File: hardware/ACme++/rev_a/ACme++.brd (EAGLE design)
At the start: 72.6 x 47.1 mm, 52 parts, among them J1 AC-PLUG, J2 WIRE_HOLE-14AWG, J4 WIRE_HOLE-14AWG, J5 WIRE_HOLE-14AWG, K1 S216S01F, Q1 STGD5NB120SZT4, Q2 FDV301N, U1 ADE7753, U2 SR086SG-G, U3 TDA3664AT, X1 ECS-35-17-5PX-TR

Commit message: working on routing
power supply laid out

working on ace

lots of room...put cc2538 on this board? hard to argue not to...
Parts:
- moved X1 29.0 mm to (15.2, 17.8)
- moved L3 25.2 mm to (34.8, 45.6), turned to 180 degrees
- moved R15 23.4 mm to (46.1, 37.7), turned to 180 degrees
- moved L4 22.7 mm to (48.4, 33.3), turned to 180 degrees
- moved C23 21.6 mm to (46.1, 35.7)
- moved R14 21.0 mm to (43.2, 34.2), turned to 90 degrees
- moved R13 18.7 mm to (34.0, 42.5), turned to 270 degrees
- moved C22 18.3 mm to (36.1, 42.5), turned to 90 degrees
- moved Q2 15.1 mm to (33.8, 16.1)
- moved R5 10.9 mm to (36.4, 11.8)
- moved R4 10.8 mm to (42.2, 11.8)
- moved R17 10.0 mm to (39.4, 2.67)
- moved C11 9.81 mm to (29.0, 10.4), turned to 180 degrees
- moved R10 9.41 mm to (31.2, 16.0), turned to 270 degrees
- moved D1 8.92 mm to (33.8, 20.3)
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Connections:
- net N$1 renamed DC_RECTIFIED
- net N$19 renamed SR086_VIN
- net N$22 renamed SR086_GATE
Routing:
- net WALL_PHASE: track 0.00 -> 49.0 mm
- net EARTH_GND: track 0.00 -> 35.9 mm
- net WALL_NEUTRAL: track 0.00 -> 31.2 mm
- net LOAD_NEUTRAL: track 0.00 -> 21.0 mm
- net LOAD_PHASE: track 0.00 -> 19.7 mm
- net SR086_GATE: track 0.00 -> 15.5 mm, vias 0 -> 2
- net DC_RECTIFIED: track 0.00 -> 13.1 mm
- net N$13: track 0.00 -> 10.1 mm
- net 5V0: track 0.00 -> 9.59 mm
- net N$4: track 0.00 -> 8.76 mm
- net N$26: track 0.00 -> 4.39 mm
- net V2P: track 0.00 -> 4.33 mm
- net N$17: track 0.00 -> 3.42 mm
- net N$21: track 0.00 -> 2.92 mm
- net N$14: track 0.00 -> 2.58 mm
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- added copper zone on layer 1, net 5V0
- added copper zone on layer 1, net DC_RECTIFIED
- added copper zone on layer 1, net SR086_VIN
- added copper zone on layer 1, net VDC

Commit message: routing the cc2538
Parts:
- removed JP1: (no value), pinhead:1X12
- added A1: FRACTUS-2.4GHZ-FR05-S1-N-0-001, chips:FRACTUS-ANTENNA-FR05-S1-N-0-001
- added B1: 2450BM15A0002, chips:2450BM
- added C12, C16: 12pF, passives:0402_CAP
- added C18, C29, C30: 1uF, passives:0402_CAP
- added C19, C20, C21, C24, C25, C27, C28, C31: 0.1uF, passives:0402_CAP
- added C26: 220pF, passives:0402_CAP
- added C32: 1nF, passives:0402_CAP
- added C33, C34: 22pF, passives:0402_CAP
- added J3: TC2030-CTX-NL, connector:TC2030-IDC-NL
- added R16, R19, R3: 4.7k, passives:0402_RES
- added R20, R22: 2.2k, passives:0402_RES
- added R21: 56k, passives:0402_RES
- added U4: FM25LBTDFN-8, chips:TDFN-8
- added U5: CC2538, chips:S-PVQFN-N56
- added U6: DS2411, chips:SOT-23
- added X2: EPSON-FA-128, crystals:FA-128
- added X3: FC-12M32.7680KA-A3, crystals:FC-12M
- moved X1 28.0 mm to (24.1, 44.3), turned to 0 degrees
- moved C14 25.8 mm to (33.3, 40.4), turned to 90 degrees
- moved C17 25.8 mm to (33.1, 44.8), turned to 270 degrees
- moved C9 23.6 mm to (31.5, 40.4), turned to 90 degrees
- moved C3 23.4 mm to (34.5, 34.2), turned to 90 degrees
- moved R6 22.9 mm to (33.5, 31.5), turned to 180 degrees
- moved C4 21.7 mm to (32.5, 34.2), turned to 90 degrees
- moved C2 19.2 mm to (30.6, 30.1), turned to 270 degrees
- moved C1 17.4 mm to (28.6, 30.1), turned to 270 degrees
- moved R8 16.2 mm to (26.5, 30.1), turned to 90 degrees
- moved C15 15.7 mm to (18.8, 41.0), turned to 180 degrees
- moved U1 10.5 mm to (26.0, 37.0), turned to 180 degrees
- moved L3 3.14 mm to (37.8, 44.8)
- moved C22 2.29 mm to (36.2, 40.3), turned to 0 degrees
- moved R13 2.17 mm to (36.2, 42.3), turned to 180 degrees
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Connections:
- removed net GPIOUNDECIDED: JP1.10
- removed net N$12: JP1.9
- new net !FRAM_CS: R3.1, U4.1, U5.8
- new net !FRAM_HOLD: R16.1, U4.7, U5.13
- new net !FRAM_WP: R19.1, U4.3, U5.7
- new net ANTENNA: A1.1, B1.1
- new net DS2411: R22.1, U5.14, U6.1
- new net LED??: U5.51
- new net N$1: C29.1, C30.1, U5.32, U5.56
- new net N$10: C16.1, U5.35, X2.3
- new net N$2: C32.1, R20.2, U5.28
- new net N$6: C34.1, U5.45, X3.2
- new net N$7: C33.1, U5.44, X3.1
- new net N$8: R21.1, U5.42
- new net N$9: C12.1, U5.34, X2.1
- new net RF_N: B1.3, U5.38
- new net RF_P: B1.4, U5.37
- new net SCK: U4.6, U5.12
- new net TCK: J3.4, U5.47
- new net TDI: U5.49
- new net TDO: J3.6, U5.48
- new net TMS: J3.2, U5.46
- new net V_TIMER: U5.16
- net !ADE_CS: now also U5.53; no longer JP1.4
- net !ADE_IRQ: now also U5.54; no longer JP1.5
- net !RESET: now also J3.3, R20.1
- net 3V3: now also C18.1, C19.1, C20.1, C21.1, C24.1, C25.1, C26.1, C27.1, C28.1, C31.1, J3.1, R16.2, R19.2, R22.2, R3.2, U4.8, U5.10, U5.15, U5.24, U5.33, U5.36, U5.39, U5.40, U5.41, U5.43, U5.55, U6.2; no longer JP1.11
- net ADE_CF: now also U5.6; no longer JP1.7
- net ADE_ZX: now also U5.5; no longer JP1.6
- net GND: now also B1.2, B1.5, B1.6, C12.2, C16.2, C18.2, C19.2, C20.2, C21.2, C24.2, C25.2, C26.2, C27.2, C28.2, C29.2, C30.2, C31.2, C32.2, C33.2, C34.2, J3.5, R21.2, U4.4, U5.VSS_QFN, U6.3, X2.2, X2.4; no longer JP1.12
- net MISO: now also U4.2, U5.9; no longer JP1.2
- net MOSI: now also U4.5, U5.11; no longer JP1.1
- net RELAY_CTRL: now also U5.50
- net SCLK: no longer JP1.3
- net USER_RELAY_CTRL: now also U5.52; no longer JP1.8
- net WALL_NEUTRAL: now also J1.N12
- net WALL_PHASE: no longer J1.N12
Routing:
- net 3V3: track 2.02 -> 34.2 mm
- net V1N: track 2.03 -> 29.1 mm, vias 0 -> 2
- net MOSI: track 0.00 -> 25.2 mm, vias 0 -> 2
- net MISO: track 0.00 -> 20.5 mm, vias 0 -> 2
- net ADE_ZX: track 0.00 -> 20.3 mm
- net LOAD_NEUTRAL: track 21.0 -> 40.6 mm, vias 0 -> 1
- net USER_RELAY_CTRL: track 0.00 -> 19.5 mm, vias 0 -> 2
- net ADE_CF: track 0.00 -> 18.8 mm
- net N$15: track 0.00 -> 16.5 mm
- net V2P: track 4.33 -> 19.4 mm, vias 0 -> 2
- net !ADE_IRQ: track 0.00 -> 14.6 mm
- net N$3: track 0.00 -> 14.2 mm
- net !ADE_CS: track 0.00 -> 13.7 mm
- net 5V0: track 9.59 -> 21.8 mm
- net !FRAM_WP: track 0.00 -> 11.7 mm
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
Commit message: working on ground plane
man there are some rediculous traces for this cc2538
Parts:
- added D4, D7: GREEN, SparkFun-LED:LED-0603
- added D6: RED, SparkFun-LED:LED-0603
- added R23, R24, R25: 470, passives:0402_RES
- added U7: TXB0104RGY, chips:S-PVQFN-N14
- moved C20 2.88 mm to (4.32, 30.2), turned to 90 degrees
- moved C34 1.30 mm to (18.2, 22.1)
- moved C21 1.22 mm to (7.49, 32.1)
- moved C32 1.02 mm to (1.65, 22.5), turned to 90 degrees
- moved R22 1.02 mm to (2.11, 30.4)
- moved U6 0.89 mm to (2.11, 32.6)
- moved C18 0.81 mm to (14.5, 29.9)
- moved C30 0.81 mm to (13.4, 29.9)
- moved C33 0.80 mm to (18.2, 21.1)
- moved X3 0.80 mm to (16.4, 21.8)
- moved R16 0.76 mm to (4.90, 35.7), turned to 270 degrees
- moved C19 0.64 mm to (2.16, 24.0)
- moved R20 0.57 mm to (2.67, 22.5), turned to 270 degrees
- moved C2 0.54 mm to (30.2, 30.5)
- moved R8 0.40 mm to (26.7, 30.5)
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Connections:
- removed net LED??: U5.51
- removed net SCK: U4.6, U5.12
- removed net V_TIMER: U5.16
- new net !ADE_CS_5V: U1.17, U7.13
- new net GREEN_LED: D7.C, U5.22
- new net MISO_5V: U1.19, U7.11
- new net MOSI_5V: U1.20, U7.10
- new net N$12: D4.A, R25.2
- new net N$20: D6.A, R23.2
- new net N$22: D7.A, R24.2
- new net RED_LED: D6.C, U5.23
- new net RELAY_LED: D4.C, U5.51
- new net SCLK_5V: U1.18, U7.12
- net !ADE_CS: now also U7.2; no longer U1.17
- net 3V3: now also R23.1, R24.1, R25.1, U7.1, U7.8
- net 5V0: now also U7.14
- net GND: now also U7.7, U7.THERMALPAD
- net MISO: now also U7.4; no longer U1.19
- net MOSI: now also U7.5; no longer U1.20
- net SCLK: now also U4.6, U5.12, U7.3; no longer U1.18
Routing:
- net 3V3: track 34.2 -> 151.6 mm, vias 0 -> 14
- net !RESET: track 5.11 -> 31.1 mm, vias 0 -> 2
- net RELAY_CTRL: track 1.64 -> 26.5 mm, vias 0 -> 4
- net 5V0: track 21.8 -> 46.6 mm, vias 0 -> 2
- net SCLK: track 0.00 -> 22.7 mm, vias 0 -> 3
- net RELAY_LED: track 0.00 -> 12.7 mm, vias 0 -> 2
- net SCK: track 8.64 -> 0.00 mm, vias 2 -> 0
- net DS2411: track 1.50 -> 7.62 mm, vias 0 -> 2
- net MISO: track 20.5 -> 15.0 mm
- net MOSI: track 25.2 -> 19.6 mm
- net !ADE_IRQ: track 14.6 -> 18.5 mm
- net GREEN_LED: track 0.00 -> 3.87 mm
- net RED_LED: track 0.00 -> 3.03 mm
- net USER_RELAY_CTRL: track 19.5 -> 22.3 mm
- net !ADE_CS_5V: track 0.00 -> 1.89 mm
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- added copper zone on layer 1, net GND
- added copper zone on layer 16, net GND

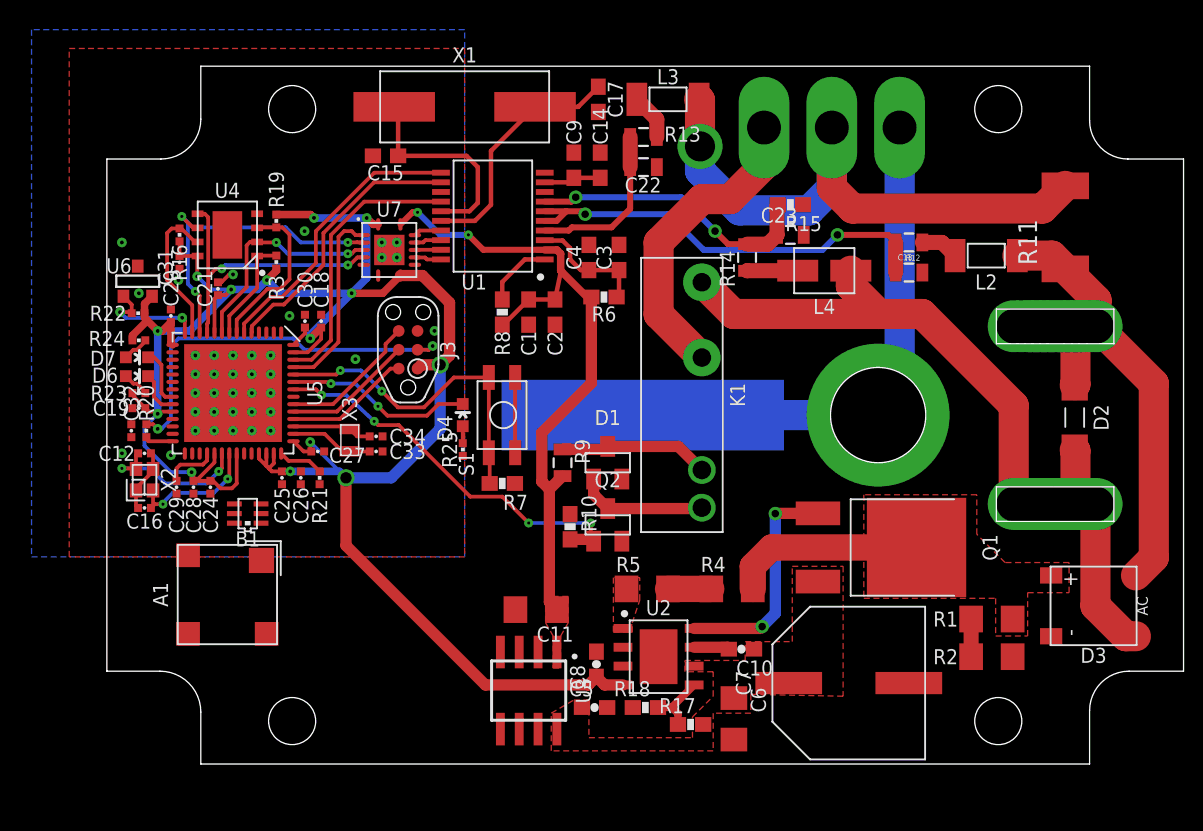
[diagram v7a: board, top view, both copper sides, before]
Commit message: routed.
still not sure what to do with "GND" for the differential signals
running to the ade
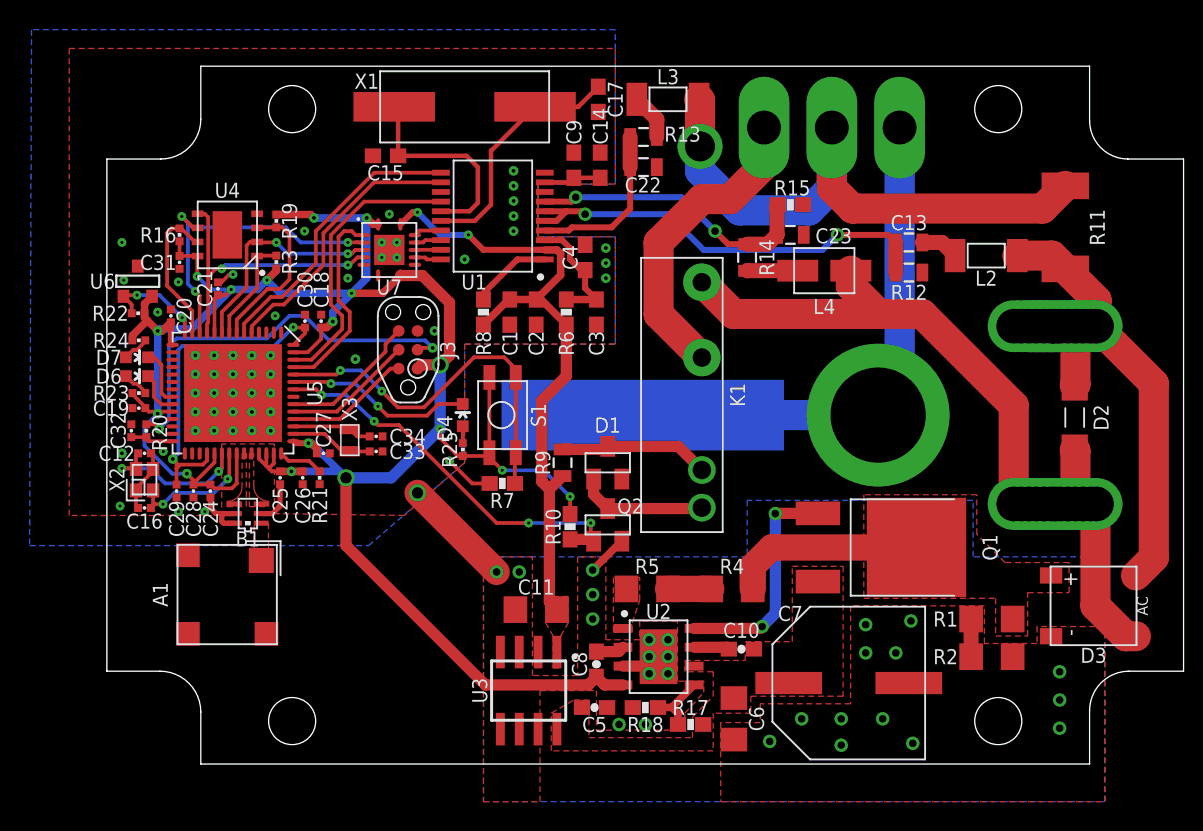
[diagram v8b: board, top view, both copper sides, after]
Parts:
- moved C3 3.99 mm to (33.0, 30.5), turned to 270 degrees
- moved R6 2.74 mm to (31.0, 30.5), turned to 270 degrees
- moved R8 1.27 mm to (25.4, 30.5)
- moved C1 1.27 mm to (27.2, 30.5)
- moved C2 1.27 mm to (29.0, 30.5)
- moved C27 0.40 mm to (14.6, 21.0)
- moved C24 0.25 mm to (6.99, 18.4)
- moved C28 0.25 mm to (5.84, 18.4)
- moved C29 0.25 mm to (4.70, 18.4)
- moved C4 0.25 mm to (32.3, 34.2)
- moved C25 0.13 mm to (11.7, 19.3)
- moved C26 0.13 mm to (13.2, 19.3)
- turned R7 to 0 degrees
- turned S1 to 270 degrees
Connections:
- new net !ADE_RESET: R8.2, U1.1
- new net N$19: C22.2
- new net N$23: C13.2
- new net N$25: C23.2
- new net N$27: R15.1
- net !RESET: no longer R8.2, U1.1
- net GND: no longer C13.2, C22.2, C23.2, R15.1
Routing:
- net GND: track 5.51 -> 30.7 mm, vias 39 -> 82
- net N$1: track 5.08 -> 22.8 mm, vias 0 -> 2
- net 3V3: track 151.6 -> 162.5 mm, vias 14 -> 17
- net WALL_NEUTRAL: track 31.2 -> 36.8 mm
- net WALL_PHASE: track 49.0 -> 54.6 mm
- net !ADE_RESET: track 0.00 -> 5.50 mm
- net !RESET: track 31.1 -> 27.5 mm
- net USER_RELAY_CTRL: track 22.3 -> 25.6 mm
- net 5V0: track 46.6 -> 44.6 mm
- net N$2: track 1.94 -> 2.96 mm
- net !ADE_IRQ: track 18.5 -> 19.2 mm
- net !ADE_CS: track 12.8 -> 13.4 mm
- net DS2411: track 7.62 -> 7.08 mm
- added copper zone on layer 1, net ANTENNA
- added copper zone on layer 1, net RF_N
- added copper zone on layer 1, net RF_P
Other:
- outline, holes or cut-outs redrawn
